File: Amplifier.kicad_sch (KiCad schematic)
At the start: 8 parts, among them J15 Conn_02x04_Odd_Even, U3 MAX98357A

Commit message: Add Robot-Adapter and OEM plugs WIP
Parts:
- removed J15: Conn_02x04_Odd_Even, Connector_PinHeader_2.54mm:PinHeader_2x04_P2.54mm_Vertical, symbol Connector_Generic:Conn_02x04_Odd_Even

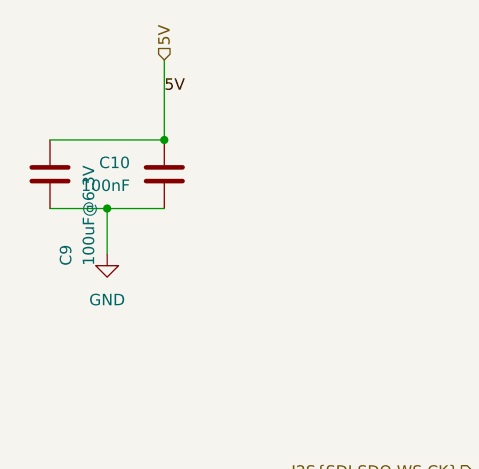
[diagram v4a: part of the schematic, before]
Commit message: Fix BOM and switch C0402 to C0603
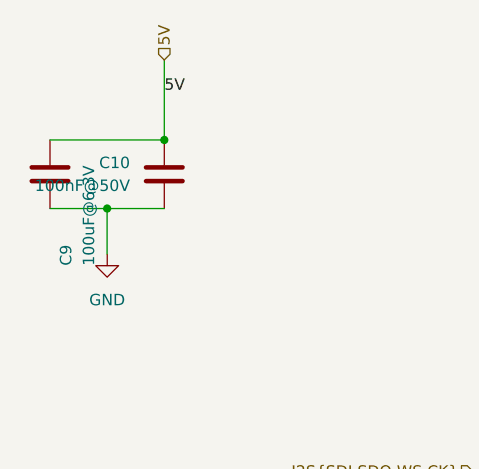
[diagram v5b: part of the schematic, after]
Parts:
- C10: value 100nF -> 100nF@50V; footprint Capacitor_SMD:C_0402_1005Metric -> Capacitor_SMD:C_0603_1608Metric; JLC C307331 -> C14663
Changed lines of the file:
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@@
 			)
 		)
-		(property "Value" "100nF"
+		(property "Value" "100nF@50V"
 			(at 57.15 62.2299 0)
 			(effects
@@
 			)
 		)
-		(property "Footprint" "Capacitor_SMD:C_0402_1005Metric"
+		(property "Footprint" "Capacitor_SMD:C_0603_1608Metric"
 			(at 61.9252 57.15 0)
 			(effects
@@
 			)
 		)
-		(property "JLC" "C307331"
+		(property "JLC" "C14663"
 			(at 60.96 60.96 0)
 			(effects

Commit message: Fix BOM and parts placement
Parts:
- U3: FT Rotation Offset (none) -> -90
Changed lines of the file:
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@@
 			)
 		)
-		(property "APPLICATION" ""
+		(property "FT Rotation Offset" "-90"
 			(at 152.4 109.22 0)
 			(effects
